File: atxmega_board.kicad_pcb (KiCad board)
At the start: 2 copper layers, 41 x 30 mm, 28 parts, among them CON1 USB, IC1 ATXMEGA, P1 PDI, P2 PORTD, P3 PORTA, P4 PORTC, P5 PORTB, P6 PORTE, SW1 SW_PUSH, X1 CRYSTAL_SMD

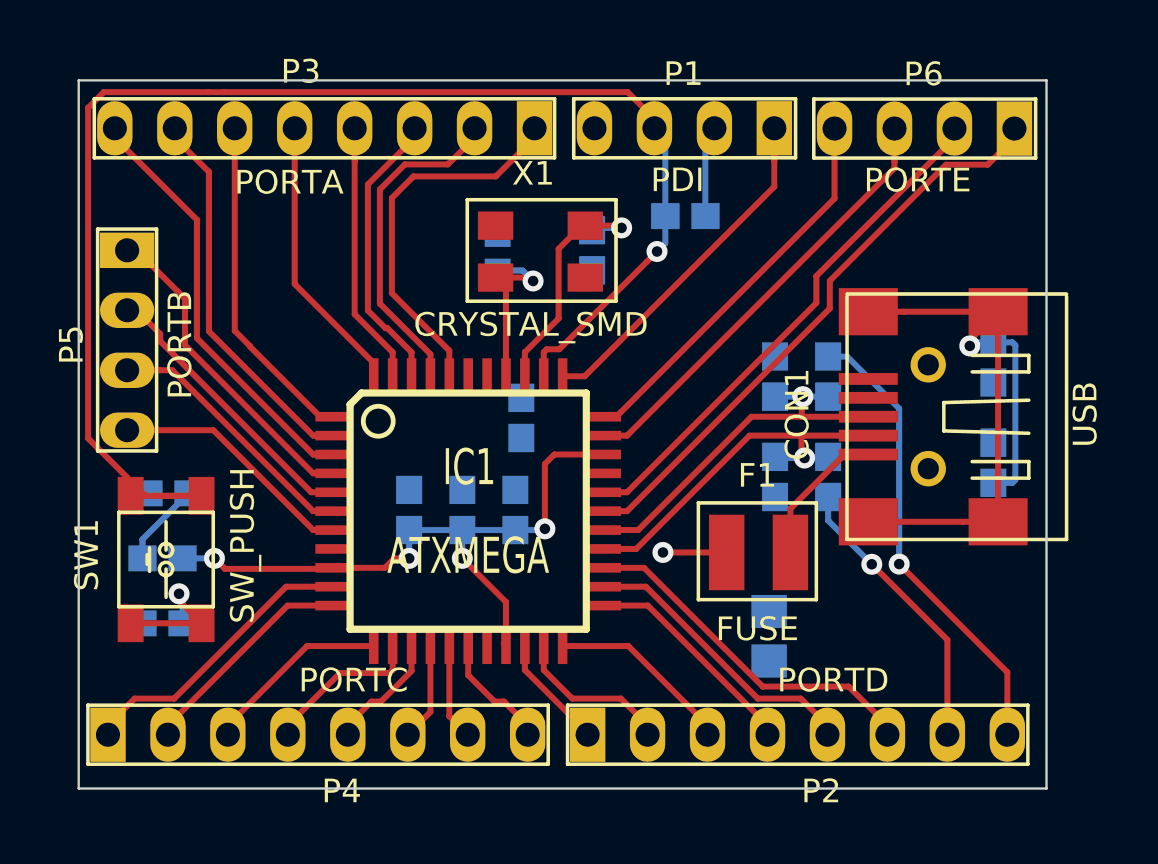
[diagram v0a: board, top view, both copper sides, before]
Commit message: Round edges
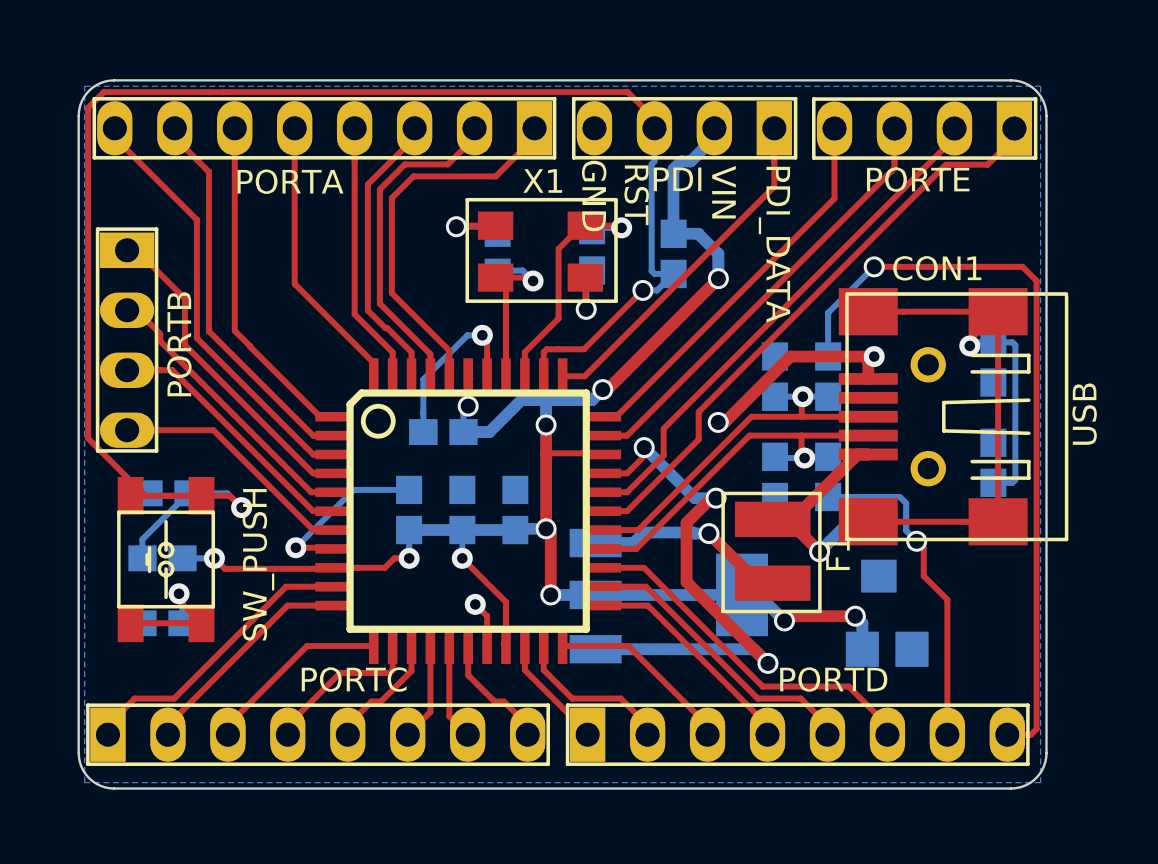
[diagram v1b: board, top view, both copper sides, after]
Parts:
- added C10: 4.7u, buq2:SM0805, B.Cu at (47.2, 37.1)
- added U1: NCP1117ST33T3G, buq2:SOT-223, B.Cu at (34.9, 37.1)
- moved C5 5.88 mm to (46.9, 32.9)
- moved C6 3.31 mm to (28.5, 27.9), turned to 0 degrees
- moved R4 1.64 mm to (38.2, 20.3), turned to 90 degrees
- moved F1 0.65 mm to (42.4, 33.0), turned to 270 degrees
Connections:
- F1 pad 2: VIN -> Net-(F1-Pad2)
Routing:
- net GND: track 0.85 -> 55.4 mm, vias 0 -> 10
- net VIN: track 35.6 -> 75.2 mm, vias 5 -> 11
- net PD7: track 19.6 -> 32.5 mm
- net Net-(F1-Pad2): track 0.00 -> 8.58 mm, vias 0 -> 1
- net RST: track 64.6 -> 71.5 mm, vias 1 -> 2
- net VBUS: track 6.11 -> 12.7 mm, vias 0 -> 1
- net PD6: track 12.2 -> 13.9 mm
- added copper zone on B.Cu, net GND
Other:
- outline, holes or cut-outs redrawn
- net class POWER added: clearance 0.254, trace_width 0.5, via_dia 0.889, via_drill 0.635
- board text added: "GND"
- board text added: "PDI_DATA"
- board text added: "RST"
- board text added: "VIN"

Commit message: Ordered from OSH Park
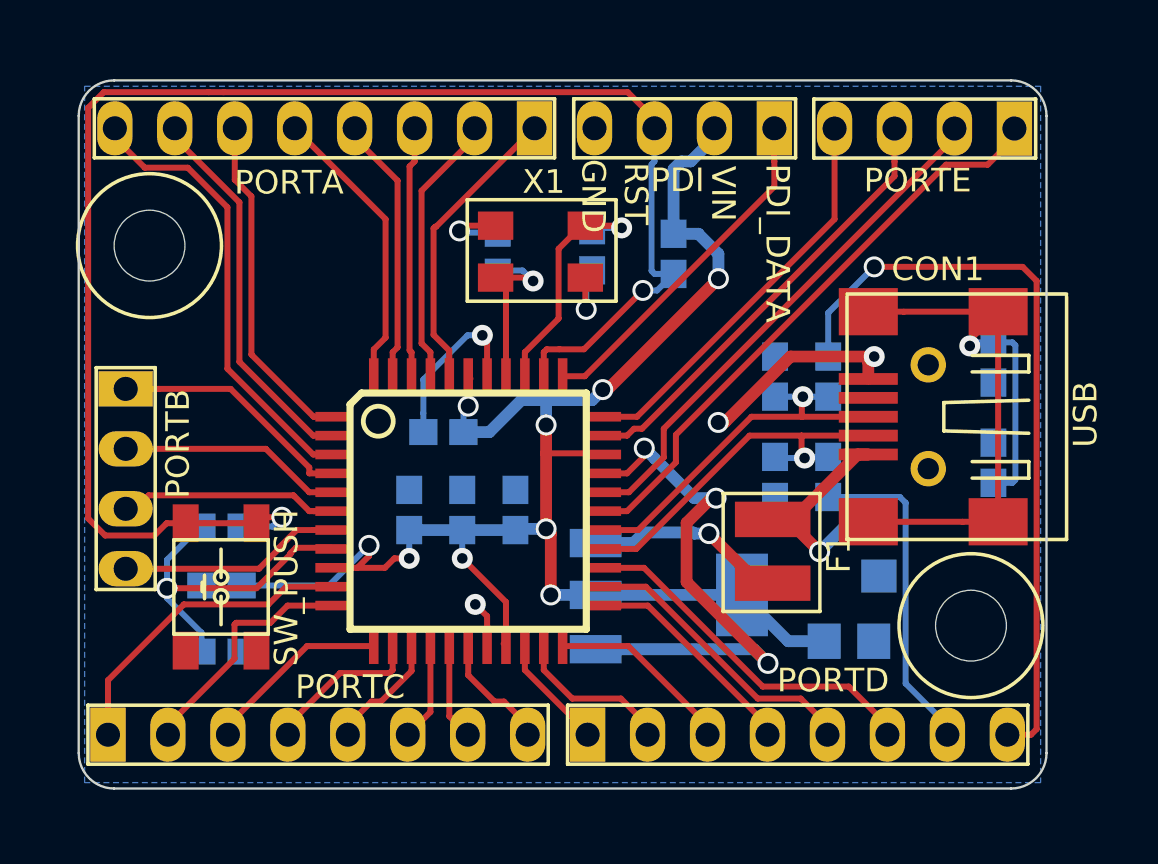
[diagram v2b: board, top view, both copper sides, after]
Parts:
- added MOUNTING_HOLE: VAL**, buq2:MOUNTING_HOLE, F.Cu at (16.0, 20.0)
- added MOUNTING_HOLE: VAL**, buq2:MOUNTING_HOLE, F.Cu at (50.8, 36.1)
- moved P5 5.87 mm to (14.9, 29.9)
- moved R2 2.77 mm to (19.0, 37.2)
- moved R3 2.75 mm to (19.0, 34.4)
- moved C4 2.65 mm to (19.0, 31.9)
- moved SW1 2.60 mm to (22.3, 37.2)
- moved C10 1.66 mm to (45.6, 36.8)
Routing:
- net GND: track 55.4 -> 62.1 mm
- net Net-(R2-Pad1): track 5.96 -> 0.00 mm, vias 1 -> 0
- net PA0: track 16.1 -> 12.6 mm
- net PB0: track 13.8 -> 10.4 mm
- net RST: track 71.5 -> 68.9 mm
- net PB1: track 12.1 -> 9.56 mm
- net PA1: track 14.1 -> 11.6 mm
- net PC0: track 12.4 -> 13.9 mm
- net PA2: track 12.1 -> 10.6 mm
- net PB3: track 10.9 -> 9.50 mm
- net VIN: track 75.2 -> 74.1 mm, vias 11 -> 9
- net PA7: track 18.2 -> 19.2 mm
- net PB2: track 11.2 -> 10.2 mm
- net PC1: track 9.50 -> 10.4 mm
- net PE3: track 16.6 -> 17.1 mm
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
